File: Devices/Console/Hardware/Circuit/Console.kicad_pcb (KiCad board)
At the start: 2 copper layers, 4 parts, among them J1 AVR-ISP-6, J2 U254-051T-4BH83-F1S, SW1 PEC11R-4220F-S0012, U1 ATmega328P-AU

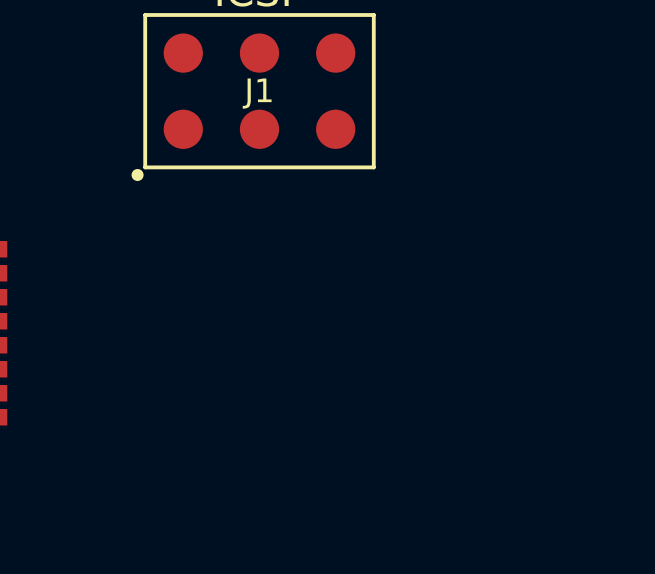
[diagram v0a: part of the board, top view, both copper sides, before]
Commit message: Exchange Micro USB with Type C
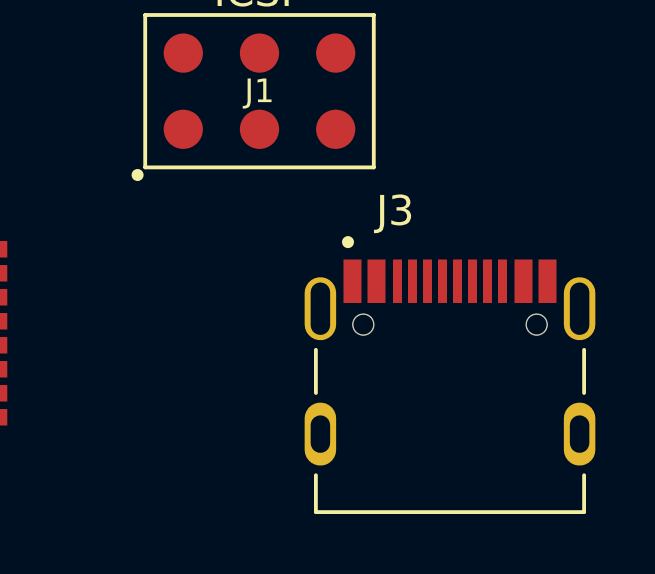
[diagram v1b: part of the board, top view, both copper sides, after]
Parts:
- added J3: TYPE-C-31-M-12, HRO_TYPE-C-31-M-12:HRO_TYPE-C-31-M-12, F.Cu at (145.8, 80.8)

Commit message: First rough console schematic
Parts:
- removed J2: U254-051T-4BH83-F1S, XKB-U254-051T-4BH83-F1S:XKB_U254-051T-4BH83-F1S
- added C1: 22p, Capacitor_SMD:C_0805_2012Metric_Pad1.18x1.45mm_HandSolder, F.Cu at (104.0, 44.9)
- added C2: 22p, Capacitor_SMD:C_0805_2012Metric_Pad1.18x1.45mm_HandSolder, F.Cu at (108.8, 44.9)
- added C3: 100n, Capacitor_SMD:C_0805_2012Metric_Pad1.18x1.45mm_HandSolder, F.Cu at (104.0, 47.9)
- added JP1: SolderJumper, Jumper:SolderJumper-2_P1.3mm_Open_Pad1.0x1.5mm, F.Cu at (128.4, 66.0)
- added JP10: SolderJumper, Jumper:SolderJumper-2_P1.3mm_Open_Pad1.0x1.5mm, F.Cu at (130.3, 48.7)
- added JP2: SolderJumper, Jumper:SolderJumper-2_P1.3mm_Open_Pad1.0x1.5mm, F.Cu at (108.6, 48.1)
- added JP3: SolderJumper, Jumper:SolderJumper-2_P1.3mm_Open_Pad1.0x1.5mm, F.Cu at (112.9, 48.1)
- added JP4: SolderJumper, Jumper:SolderJumper-2_P1.3mm_Open_Pad1.0x1.5mm, F.Cu at (117.3, 48.1)
- added JP5: SolderJumper, Jumper:SolderJumper-2_P1.3mm_Open_Pad1.0x1.5mm, F.Cu at (121.6, 45.1)
- added JP6: SolderJumper, Jumper:SolderJumper-2_P1.3mm_Open_Pad1.0x1.5mm, F.Cu at (126.0, 45.1)
- added JP7: SolderJumper, Jumper:SolderJumper-2_P1.3mm_Open_Pad1.0x1.5mm, F.Cu at (130.3, 45.1)
- added JP8: SolderJumper, Jumper:SolderJumper-2_P1.3mm_Open_Pad1.0x1.5mm, F.Cu at (121.6, 48.7)
- added JP9: SolderJumper, Jumper:SolderJumper-2_P1.3mm_Open_Pad1.0x1.5mm, F.Cu at (126.0, 48.7)
- added R1: 10k, Resistor_SMD:R_0805_2012Metric_Pad1.20x1.40mm_HandSolder, F.Cu at (113.6, 44.8)
- added SW2: PEC11R-4220F-S0012, Bourns-PEC11R-4220F-S0012:Bourns-PEC11R-4220F-S0012-MFG, F.Cu at (109.1, 34.5)
- added SW3: PEC11R-4220F-S0012, Bourns-PEC11R-4220F-S0012:Bourns-PEC11R-4220F-S0012-MFG, F.Cu at (124.1, 34.5)
- added SW4: PEC11R-4220F-S0012, Bourns-PEC11R-4220F-S0012:Bourns-PEC11R-4220F-S0012-MFG, F.Cu at (139.1, 34.5)
- added Y1: 16MHz, Crystal:Crystal_SMD_HC49-SD_HandSoldering, F.Cu at (137.3, 59.6)
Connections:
- J1 pad 1: Net-(J1-Pad1) -> /MISO
- J1 pad 2: Net-(J1-Pad2) -> VCC
- J1 pad 3: Net-(J1-Pad3) -> /SCK
- J1 pad 4: Net-(J1-Pad4) -> /MOSI
- J1 pad 5: Net-(J1-Pad5) -> /RST
- J1 pad 6: Net-(J1-Pad6) -> GND
- J3 pad A1B12: Net-(J3-PadA1B12) -> GND
- J3 pad A4B9: Net-(J3-PadA4B9) -> VCC
- J3 pad B1A12: Net-(J3-PadB1A12) -> GND
- J3 pad B4A9: Net-(J3-PadB4A9) -> VCC
- J3 pad S1: Net-(J3-PadS1) -> GND
- J3 pad S2: Net-(J3-PadS2) -> GND
- J3 pad S3: Net-(J3-PadS3) -> GND
- J3 pad S4: Net-(J3-PadS4) -> GND
- SW1 pad A: Net-(SW1-PadA) -> /ENC1A
- SW1 pad B: Net-(SW1-PadB) -> /ENC1B
- SW1 pad C: Net-(SW1-PadC) -> GND
- SW1 pad S1: Net-(SW1-PadS1) -> GND
- SW1 pad S2: Net-(SW1-PadS2) -> /BTN1
- U1 pad 1: Net-(U1-Pad1) -> /ENC1B
- U1 pad 10: Net-(U1-Pad10) -> /ENC3A
- U1 pad 11: Net-(U1-Pad11) -> /ENC3B
- U1 pad 12: Net-(U1-Pad12) -> /ENC4A
- U1 pad 13: Net-(U1-Pad13) -> /ENC4B
- U1 pad 15: Net-(U1-Pad15) -> /MOSI
- U1 pad 16: Net-(U1-Pad16) -> /MISO
- U1 pad 17: Net-(U1-Pad17) -> /SCK
- U1 pad 18: Net-(U1-Pad18) -> VCC
- U1 pad 2: Net-(U1-Pad2) -> /ENC2A
- U1 pad 21: Net-(U1-Pad21) -> GND
- U1 pad 23: Net-(U1-Pad23) -> /BTN1
- U1 pad 24: Net-(U1-Pad24) -> /BTN2
- U1 pad 25: Net-(U1-Pad25) -> /BTN3
- U1 pad 26: Net-(U1-Pad26) -> /BTN4
- U1 pad 27: Net-(U1-Pad27) -> /SDA
- U1 pad 28: Net-(U1-Pad28) -> /SCL
- U1 pad 29: Net-(U1-Pad29) -> /RST
- U1 pad 3: Net-(U1-Pad21) -> GND
- U1 pad 30: Net-(U1-Pad30) -> /RX
- U1 pad 31: Net-(U1-Pad31) -> /TX
- U1 pad 32: Net-(U1-Pad32) -> /ENC1A
- U1 pad 4: Net-(U1-Pad4) -> VCC
- U1 pad 5: Net-(U1-Pad21) -> GND
- U1 pad 6: Net-(U1-Pad4) -> VCC
- U1 pad 7: Net-(U1-Pad7) -> /XTAL1
- U1 pad 8: Net-(U1-Pad8) -> /XTAL2
- U1 pad 9: Net-(U1-Pad9) -> /ENC2B

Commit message: Add communication breakout pins
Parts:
- added J2: Conn_01x13, Connector_PinHeader_1.00mm:PinHeader_1x13_P1.00mm_Vertical, F.Cu at (159.3, 35.3)
- added J4: Conn_01x04, Connector_PinHeader_1.00mm:PinHeader_1x04_P1.00mm_Vertical, F.Cu at (160.7, 55.4)
- added J5: Conn_01x04, Connector_PinHeader_1.00mm:PinHeader_1x04_P1.00mm_Vertical, F.Cu at (164.0, 55.4)
- moved SW1 43.1 mm to (94.0, 34.3)

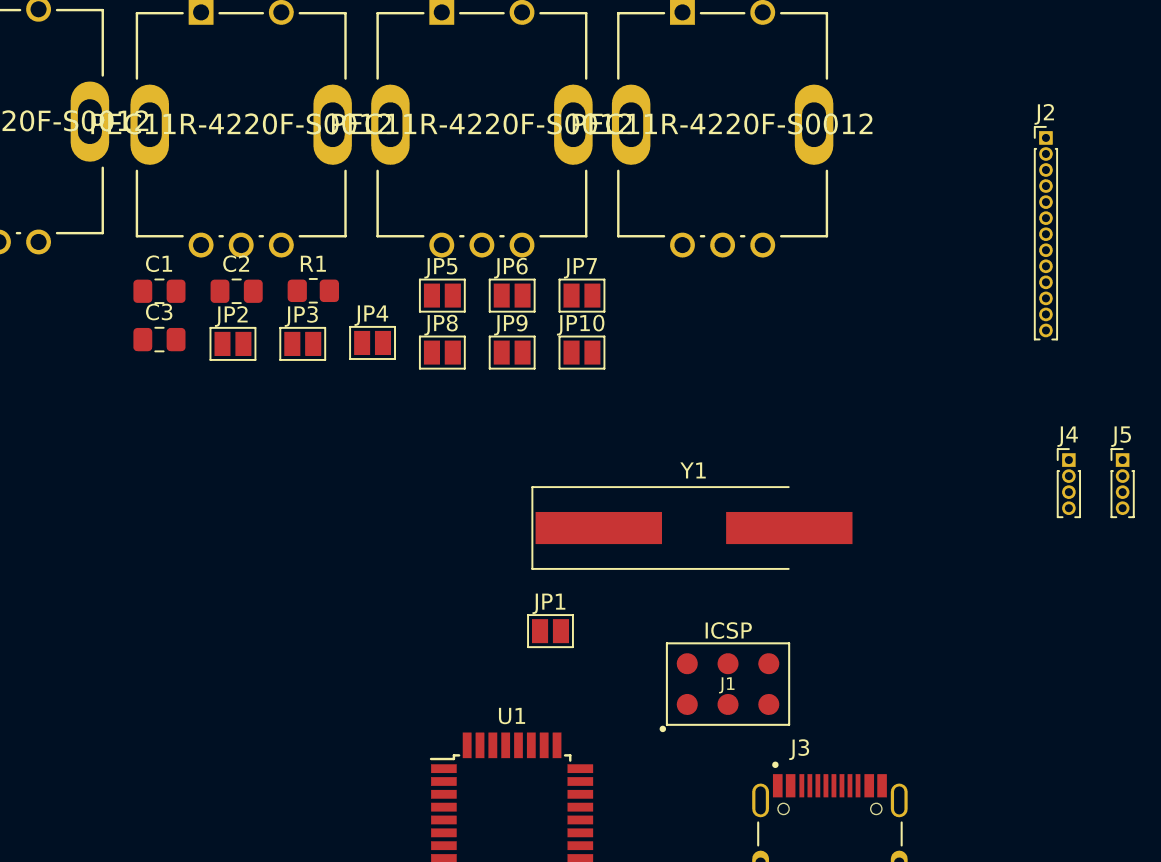
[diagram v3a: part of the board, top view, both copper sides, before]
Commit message: Change net label type to global
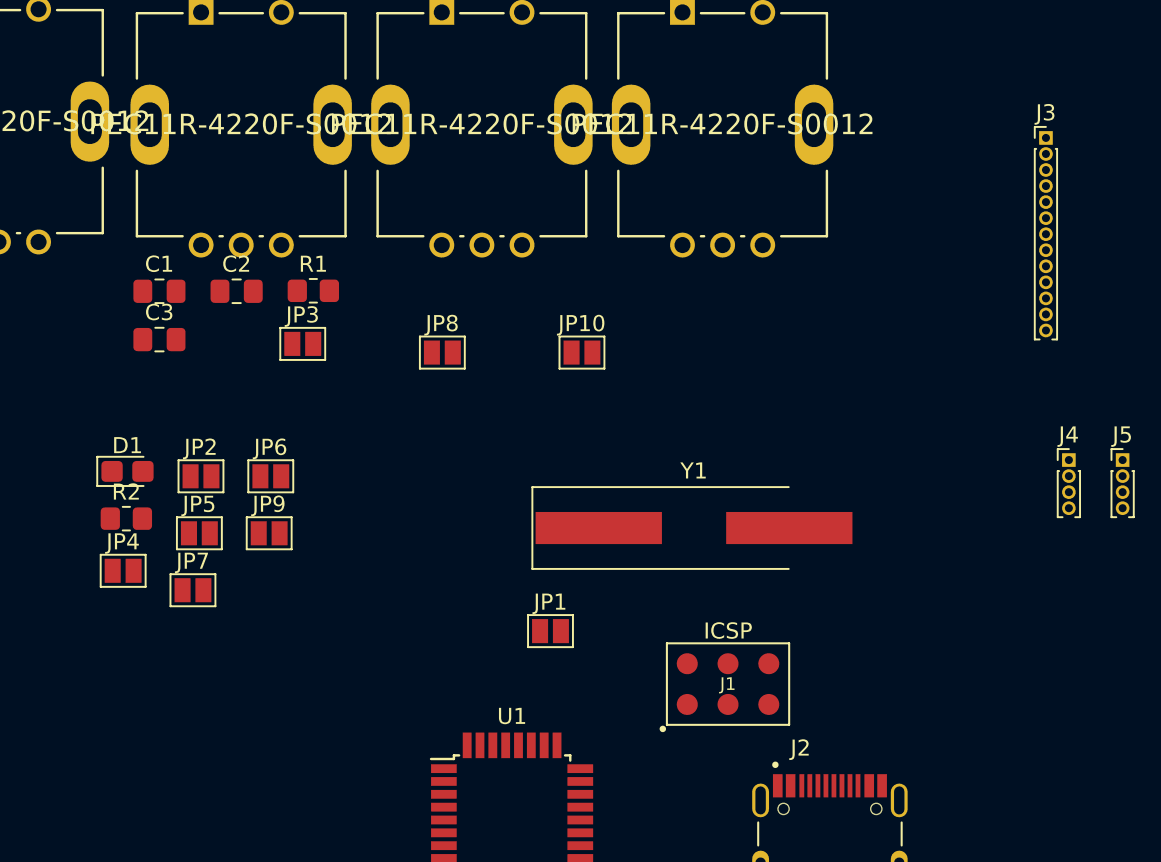
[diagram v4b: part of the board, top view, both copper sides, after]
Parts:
- added D1: 17-21/BHC-XL2M2TY/3T, LED_SMD:LED_0805_2012Metric_Castellated, F.Cu at (102.0, 56.1)
- added R2: 200, Resistor_SMD:R_0805_2012Metric_Pad1.20x1.40mm_HandSolder, F.Cu at (102.0, 59.0)
- moved JP7 30.4 mm to (106.1, 63.5)
- moved JP5 21.2 mm to (106.5, 59.9)
- moved JP4 21.1 mm to (101.8, 62.3)
- moved JP9 18.9 mm to (110.9, 59.9)
- moved JP6 18.8 mm to (111.0, 56.4)
- moved JP2 8.49 mm to (106.6, 56.4)
- renumbered J3 to J2, J2 to J3
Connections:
- net /BTN1 renamed BTN1
- net /BTN2 renamed BTN2
- net /BTN3 renamed BTN3
- net /BTN4 renamed BTN4
- net /ENC1A renamed ENC1A
- net /ENC1B renamed ENC1B
- net /ENC2A renamed ENC2A
- net /ENC2B renamed ENC2B
- net /ENC3A renamed ENC3A
- net /ENC3B renamed ENC3B
- net /ENC4A renamed ENC4A
- net /ENC4B renamed ENC4B
- net /MISO renamed MISO
- net /MOSI renamed MOSI
- net /RST renamed RST
- net /RX renamed RX
- net /SCK renamed SCK
- net /SCL renamed SCL
- net /SDA renamed SDA
- net /TX renamed TX
- net /XTAL1 renamed XTAL1
- net /XTAL2 renamed XTAL2

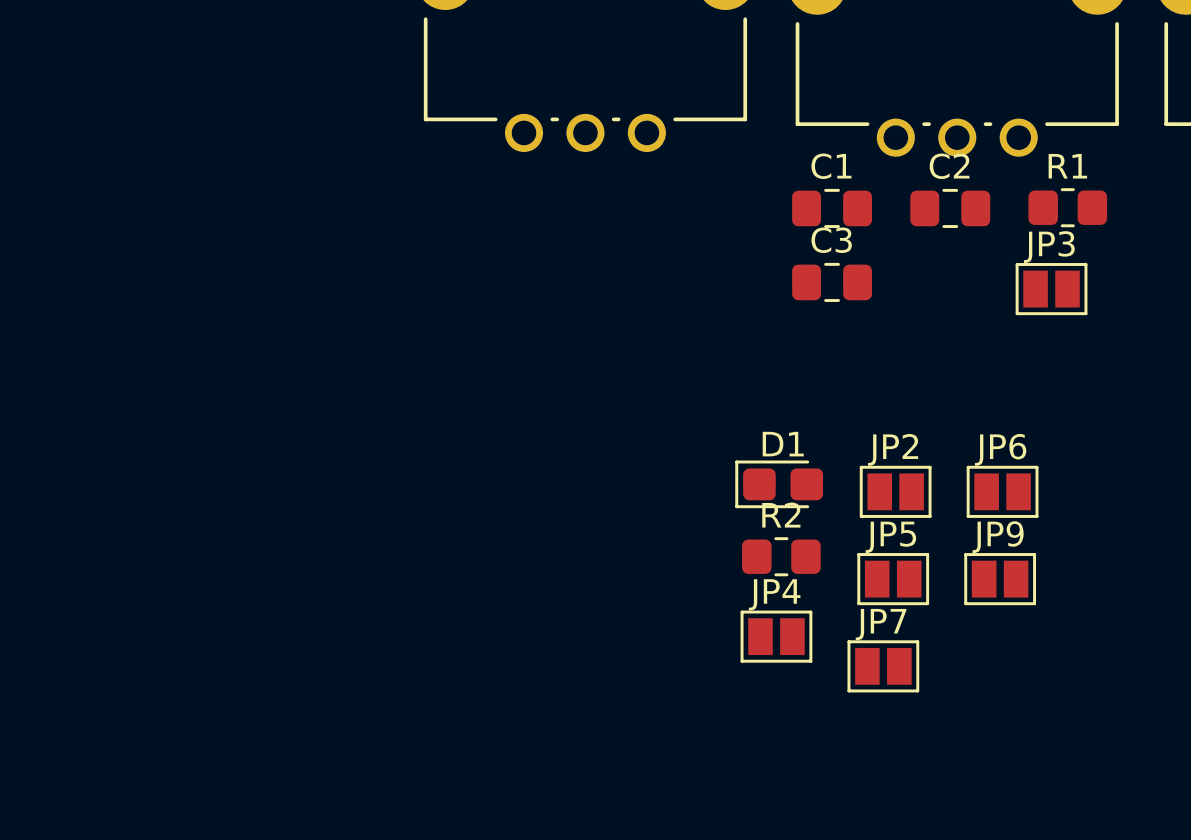
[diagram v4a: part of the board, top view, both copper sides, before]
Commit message: Change console reset button symbol + solder jumper footprint
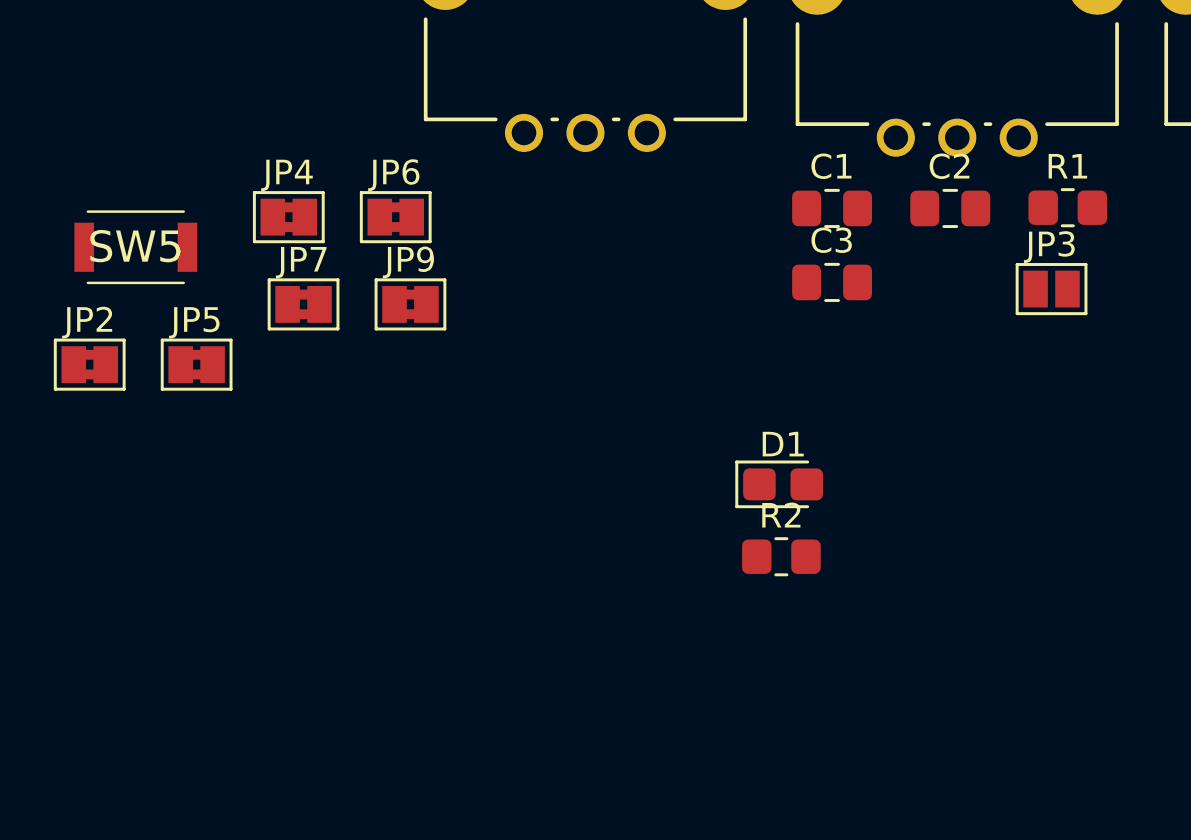
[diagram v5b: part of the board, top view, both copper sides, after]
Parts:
- added SW5: SW_Push, SKRKAEE020:SKRKAEE020, F.Cu at (75.7, 46.4)
- JP2, JP4, JP5, JP6, JP7, JP9: value SolderJumper -> SolderJumper_Bridged; footprint Jumper:SolderJumper-2_P1.3mm_Open_Pad1.0x1.5mm -> Jumper:SolderJumper-2_P1.3mm_Bridged2Bar_Pad1.0x1.5mm
- moved JP2 33.2 mm to (73.8, 51.2)
- moved JP5 29.7 mm to (78.2, 51.2)
- moved JP7 27.8 mm to (82.5, 48.8)
- moved JP6 27.1 mm to (86.3, 45.2)
- moved JP9 26.5 mm to (86.9, 48.8)
- moved JP4 26.2 mm to (81.9, 45.2)
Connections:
- JP10 pad 1: SDA -> Net-(J2-PadB6)
- JP10 pad 2: Net-(J2-PadB6) -> SDA
- JP6 pad 1: RST -> Net-(J2-PadB8)
- JP6 pad 2: Net-(J2-PadB8) -> RST
- JP7 pad 1: RX -> Net-(J2-PadB7)
- JP7 pad 2: Net-(J2-PadB7) -> RX
- JP8 pad 1: SCL -> Net-(J2-PadB7)
- JP8 pad 2: Net-(J2-PadB7) -> SCL
- JP9 pad 1: TX -> Net-(J2-PadB6)
- JP9 pad 2: Net-(J2-PadB6) -> TX

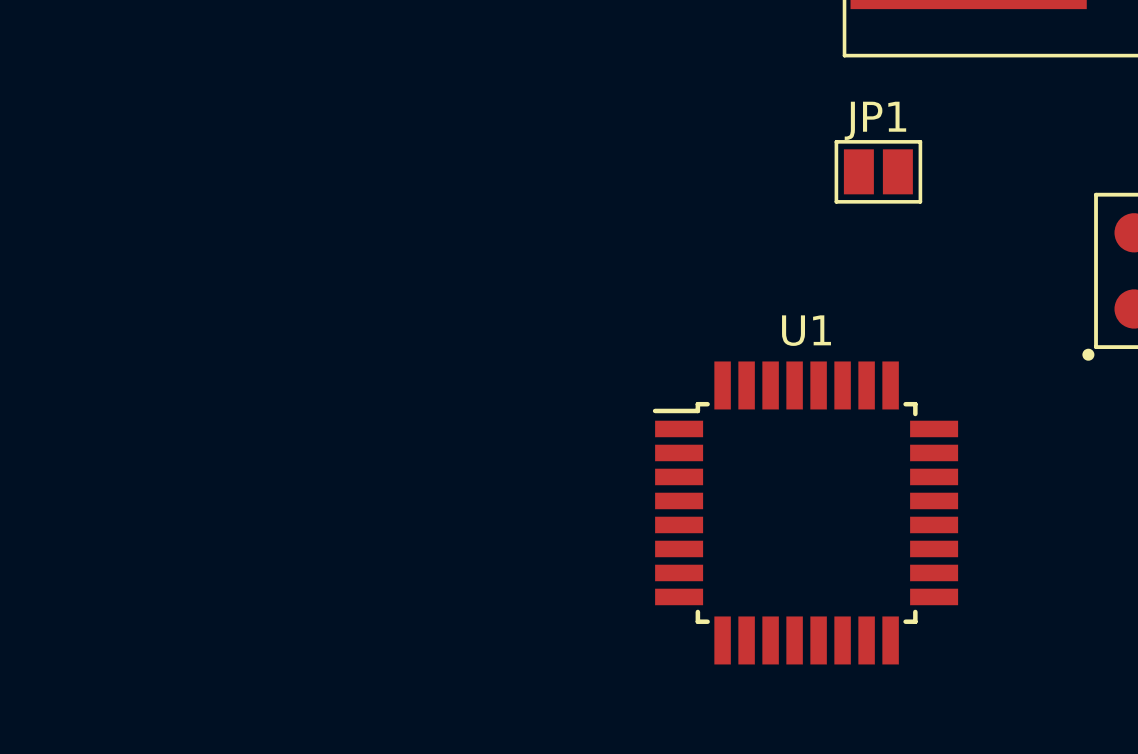
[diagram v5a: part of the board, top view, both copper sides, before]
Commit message: Add PB processor & status led to console
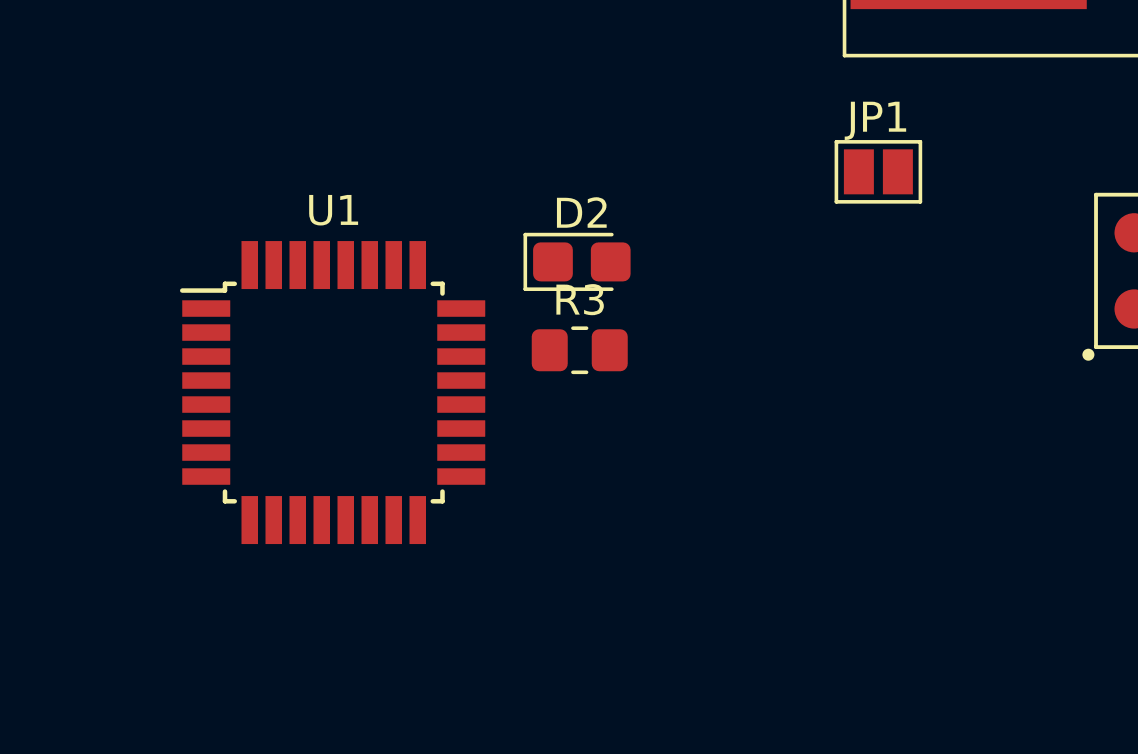
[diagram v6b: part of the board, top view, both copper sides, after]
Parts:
- added D2: 17-21/BHC-XL2M2TY/3T, LED_SMD:LED_0805_2012Metric_Castellated, F.Cu at (118.5, 69.0)
- added R3: 200, Resistor_SMD:R_0805_2012Metric_Pad1.20x1.40mm_HandSolder, F.Cu at (118.4, 72.0)
- U1: value ATmega328P-AU -> ATmega328PB-AU
- moved U1 16.3 mm to (110.2, 73.4)
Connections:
- U1 pad 14: Net-(U1-Pad14) -> LED
- U1 pad 3: GND -> Net-(U1-Pad3)
- U1 pad 6: VCC -> Net-(U1-Pad6)
